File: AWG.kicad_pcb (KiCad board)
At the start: 2 copper layers, 1 part

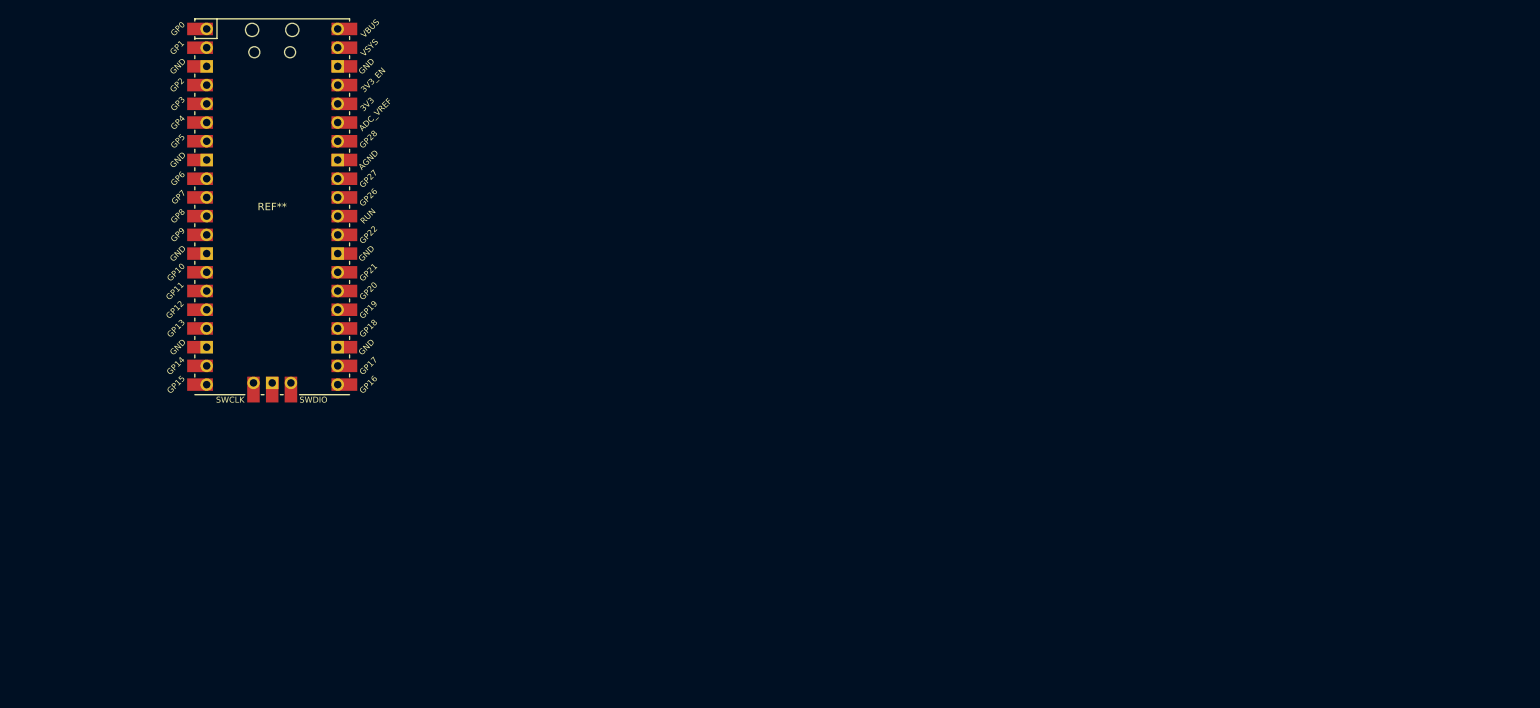
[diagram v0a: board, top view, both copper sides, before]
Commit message: 3D shapes added
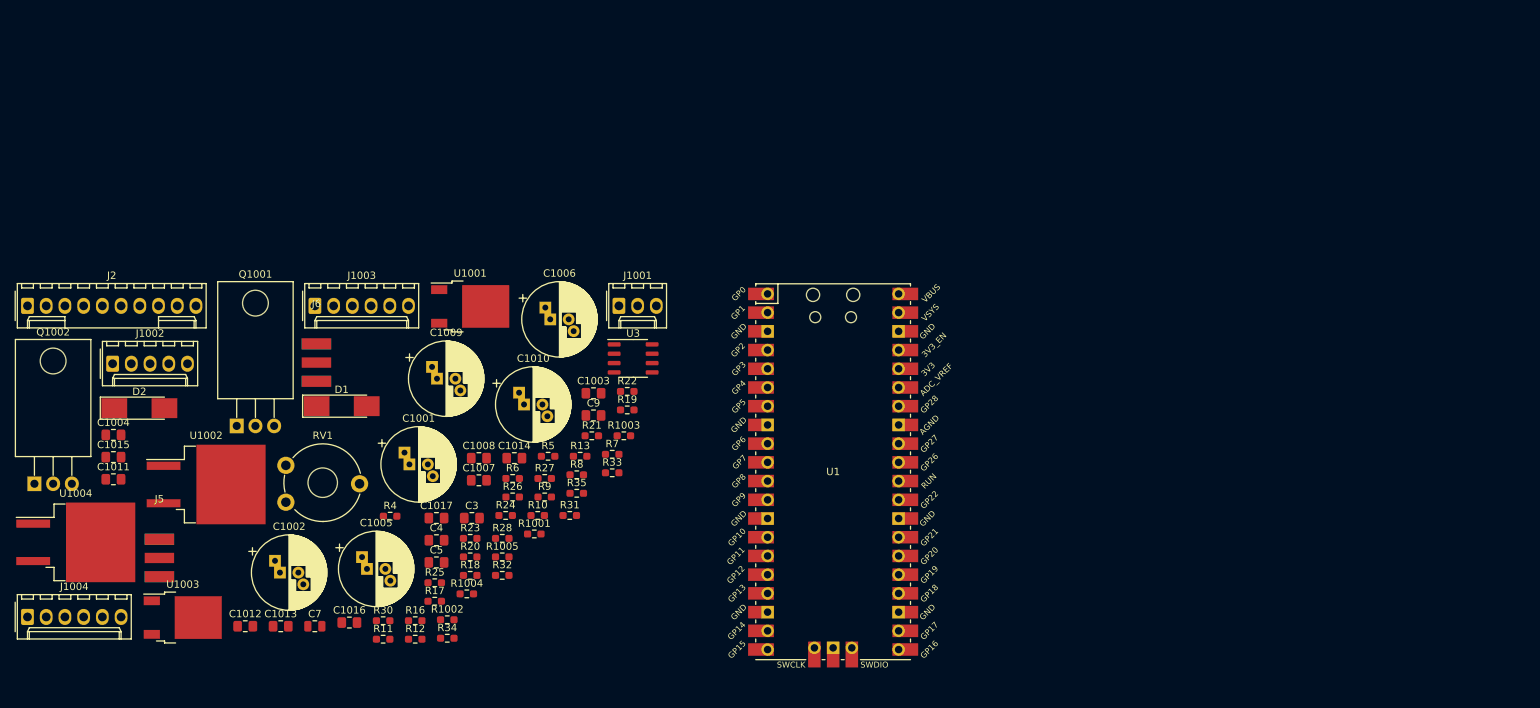
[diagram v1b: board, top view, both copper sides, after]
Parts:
- removed REF**: RPi_Pico_SMD_TH, Pi_Pico:RPi_Pico_SMD_TH
- added C1001: 100u 50V, Capacitor_THT:CP_Radial_D10.0mm_P2.50mm_P5.00mm, F.Cu at (128.6, 95.0)
- added C1002: 100u 50V, Capacitor_THT:CP_Radial_D10.0mm_P2.50mm_P5.00mm, F.Cu at (111.0, 109.6)
- added C1003: 100n, Capacitor_SMD:C_0805_2012Metric_Pad1.18x1.45mm_HandSolder, F.Cu at (153.6, 85.3)
- added C1004: 100n, Capacitor_SMD:C_0805_2012Metric_Pad1.18x1.45mm_HandSolder, F.Cu at (88.5, 91.0)
- added C1005: 100u 50V, Capacitor_THT:CP_Radial_D10.0mm_P2.50mm_P5.00mm, F.Cu at (122.9, 109.1)
- added C1006: 100u 50V, Capacitor_THT:CP_Radial_D10.0mm_P2.50mm_P5.00mm, F.Cu at (147.7, 75.3)
- added C1007: 100n, Capacitor_SMD:C_0805_2012Metric_Pad1.18x1.45mm_HandSolder, F.Cu at (138.0, 97.1)
- added C1008: 100n, Capacitor_SMD:C_0805_2012Metric_Pad1.18x1.45mm_HandSolder, F.Cu at (138.0, 94.1)
- added C1009: 100u 50V, Capacitor_THT:CP_Radial_D10.0mm_P2.50mm_P5.00mm, F.Cu at (132.4, 83.3)
- added C1010: 100u 50V, Capacitor_THT:CP_Radial_D10.0mm_P2.50mm_P5.00mm, F.Cu at (144.2, 86.8)
- added C1011: 100n, Capacitor_SMD:C_0805_2012Metric_Pad1.18x1.45mm_HandSolder, F.Cu at (88.5, 97.0)
- added C1012: 100n, Capacitor_SMD:C_0805_2012Metric_Pad1.18x1.45mm_HandSolder, F.Cu at (106.3, 116.9)
- added C1013: 100n, Capacitor_SMD:C_0805_2012Metric_Pad1.18x1.45mm_HandSolder, F.Cu at (111.2, 116.9)
- added C1014: 100n, Capacitor_SMD:C_0805_2012Metric_Pad1.18x1.45mm_HandSolder, F.Cu at (142.9, 94.1)
- added C1015: 100n, Capacitor_SMD:C_0805_2012Metric_Pad1.18x1.45mm_HandSolder, F.Cu at (88.5, 94.0)
- added C1016: 100n, Capacitor_SMD:C_0805_2012Metric_Pad1.18x1.45mm_HandSolder, F.Cu at (120.5, 116.4)
- added C1017: 100n, Capacitor_SMD:C_0805_2012Metric_Pad1.18x1.45mm_HandSolder, F.Cu at (132.3, 102.2)
- added C3: 100n, Capacitor_SMD:C_0805_2012Metric_Pad1.18x1.45mm_HandSolder, F.Cu at (137.1, 102.2)
- added C4: 100n, Capacitor_SMD:C_0805_2012Metric_Pad1.18x1.45mm_HandSolder, F.Cu at (132.3, 105.2)
- added C5: 100n, Capacitor_SMD:C_0805_2012Metric_Pad1.18x1.45mm_HandSolder, F.Cu at (132.3, 108.3)
- added C7: 3.3p, Capacitor_SMD:C_0805_2012Metric, F.Cu at (115.8, 116.9)
- added C9: 100n, Capacitor_SMD:C_0805_2012Metric_Pad1.18x1.45mm_HandSolder, F.Cu at (153.6, 88.3)
- added D1: 4148, Diode_SMD:D_MELF_Handsoldering, F.Cu at (119.4, 87.1)
- added D2: 4148, Diode_SMD:D_MELF_Handsoldering, F.Cu at (92.0, 87.3)
- added J1001: Conn_01x03, Connector_Molex:Molex_KK-254_AE-6410-03A_1x03_P2.54mm_Vertical, F.Cu at (157.0, 73.4)
- added J1002: Conn_01x05, Connector_Molex:Molex_KK-254_AE-6410-05A_1x05_P2.54mm_Vertical, F.Cu at (88.3, 81.3)
- added J1003: Conn_01x06, Connector_Molex:Molex_KK-254_AE-6410-06A_1x06_P2.54mm_Vertical, F.Cu at (115.8, 73.4)
- added J1004: Conn_01x06, Connector_Molex:Molex_KK-254_AE-6410-06A_1x06_P2.54mm_Vertical, F.Cu at (76.8, 115.7)
- added J2: Conn afficheur, Connector_Molex:Molex_KK-254_AE-6410-10A_1x10_P2.54mm_Vertical, F.Cu at (76.8, 73.4)
- added J5: SMA, SMA_PINS:SMA_EDGE_NRW, F.Cu at (94.7, 107.7)
- added J6: SMA, SMA_PINS:SMA_EDGE_NRW, F.Cu at (116.0, 81.1)
- added Q1001: NTE2633, Package_TO_SOT_THT:TO-220-3_Horizontal_TabDown, F.Cu at (105.2, 89.7)
- added Q1002: NTE2634, Package_TO_SOT_THT:TO-220-3_Horizontal_TabDown, F.Cu at (77.7, 97.6)
- added R10: 2k, Resistor_SMD:R_0603_1608Metric_Pad0.98x0.95mm_HandSolder, F.Cu at (146.0, 101.9)
- added R1001: 1k, Resistor_SMD:R_0603_1608Metric_Pad0.98x0.95mm_HandSolder, F.Cu at (145.6, 104.4)
- added R1002: 1k, Resistor_SMD:R_0603_1608Metric_Pad0.98x0.95mm_HandSolder, F.Cu at (133.8, 116.0)
- added R1003: 1k, Resistor_SMD:R_0603_1608Metric_Pad0.98x0.95mm_HandSolder, F.Cu at (157.7, 91.1)
- added R1004: 1k, Resistor_SMD:R_0603_1608Metric_Pad0.98x0.95mm_HandSolder, F.Cu at (136.4, 112.5)
- added R1005: 1k, Resistor_SMD:R_0603_1608Metric_Pad0.98x0.95mm_HandSolder, F.Cu at (141.2, 107.5)
- added R11: 2k, Resistor_SMD:R_0603_1608Metric_Pad0.98x0.95mm_HandSolder, F.Cu at (125.1, 118.7)
- added R12: 2k, Resistor_SMD:R_0603_1608Metric_Pad0.98x0.95mm_HandSolder, F.Cu at (129.4, 118.7)
- added R13: 2k, Resistor_SMD:R_0603_1608Metric_Pad0.98x0.95mm_HandSolder, F.Cu at (151.8, 93.9)
- added R16: 1k, Resistor_SMD:R_0603_1608Metric_Pad0.98x0.95mm_HandSolder, F.Cu at (129.4, 116.2)
- added R17: 1k, Resistor_SMD:R_0603_1608Metric_Pad0.98x0.95mm_HandSolder, F.Cu at (132.1, 113.5)
- added R18: 1k, Resistor_SMD:R_0603_1608Metric_Pad0.98x0.95mm_HandSolder, F.Cu at (136.9, 110.0)
- added R19: 1k, Resistor_SMD:R_0603_1608Metric_Pad0.98x0.95mm_HandSolder, F.Cu at (158.2, 87.6)
- added R20: 1k, Resistor_SMD:R_0603_1608Metric_Pad0.98x0.95mm_HandSolder, F.Cu at (136.9, 107.5)
- added R21: 1k, Resistor_SMD:R_0603_1608Metric_Pad0.98x0.95mm_HandSolder, F.Cu at (153.4, 91.1)
- added R22: 1k, Resistor_SMD:R_0603_1608Metric_Pad0.98x0.95mm_HandSolder, F.Cu at (158.2, 85.1)
- added R23: 1k, Resistor_SMD:R_0603_1608Metric_Pad0.98x0.95mm_HandSolder, F.Cu at (136.9, 105.0)
- added R24: 1k, Resistor_SMD:R_0603_1608Metric_Pad0.98x0.95mm_HandSolder, F.Cu at (141.7, 101.9)
- added R25: 2k, Resistor_SMD:R_0603_1608Metric_Pad0.98x0.95mm_HandSolder, F.Cu at (132.1, 111.0)
- added R26: 20k, Resistor_SMD:R_0603_1608Metric_Pad0.98x0.95mm_HandSolder, F.Cu at (142.6, 99.4)
- added R27: 680R, Resistor_SMD:R_0603_1608Metric_Pad0.98x0.95mm_HandSolder, F.Cu at (147.0, 96.9)
- added R28: 680R, Resistor_SMD:R_0603_1608Metric_Pad0.98x0.95mm_HandSolder, F.Cu at (141.2, 105.0)
- added R30: 27R, Resistor_SMD:R_0603_1608Metric_Pad0.98x0.95mm_HandSolder, F.Cu at (125.1, 116.2)
- added R31: 1k, Resistor_SMD:R_0603_1608Metric_Pad0.98x0.95mm_HandSolder, F.Cu at (150.4, 101.9)
- added R32: 1k, Resistor_SMD:R_0603_1608Metric_Pad0.98x0.95mm_HandSolder, F.Cu at (141.2, 110.0)
- added R33: 3R3, Resistor_SMD:R_0603_1608Metric_Pad0.98x0.95mm_HandSolder, F.Cu at (156.1, 96.1)
- added R34: 3R3, Resistor_SMD:R_0603_1608Metric_Pad0.98x0.95mm_HandSolder, F.Cu at (133.8, 118.5)
- added R35: 47R, Resistor_SMD:R_0603_1608Metric_Pad0.98x0.95mm_HandSolder, F.Cu at (151.3, 98.9)
- added R4: 2k, Resistor_SMD:R_0603_1608Metric_Pad0.98x0.95mm_HandSolder, F.Cu at (126.0, 102.0)
- added R5: 2k, Resistor_SMD:R_0603_1608Metric_Pad0.98x0.95mm_HandSolder, F.Cu at (147.4, 93.9)
- added R6: 2k, Resistor_SMD:R_0603_1608Metric_Pad0.98x0.95mm_HandSolder, F.Cu at (142.6, 96.9)
- added R7: 2k, Resistor_SMD:R_0603_1608Metric_Pad0.98x0.95mm_HandSolder, F.Cu at (156.1, 93.6)
- added R8: 2k, Resistor_SMD:R_0603_1608Metric_Pad0.98x0.95mm_HandSolder, F.Cu at (151.3, 96.4)
- added R9: 2k, Resistor_SMD:R_0603_1608Metric_Pad0.98x0.95mm_HandSolder, F.Cu at (147.0, 99.4)
- added RV1: 100R, Potentiometer_THT:Potentiometer_Piher_PT-10-V10_Vertical_Hole, F.Cu at (111.9, 100.1)
- added U1: Pico, Pi_Pico:RPi_Pico_SMD_TH, F.Cu at (186.1, 96.0)
- added U1001: L7812, Package_TO_SOT_SMD:TO-252-2, F.Cu at (136.9, 73.5)
- added U1002: L7912, Package_TO_SOT_SMD:TO-263-2, F.Cu at (101.0, 97.7)
- added U1003: L7805, Package_TO_SOT_SMD:TO-252-2, F.Cu at (97.9, 115.7)
- added U1004: L7905, Package_TO_SOT_SMD:TO-263-2, F.Cu at (83.3, 105.5)
- added U3: AD8055ARZ, Package_SO:SO-8_3.9x4.9mm_P1.27mm, F.Cu at (159.0, 80.6)

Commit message: heatsink added
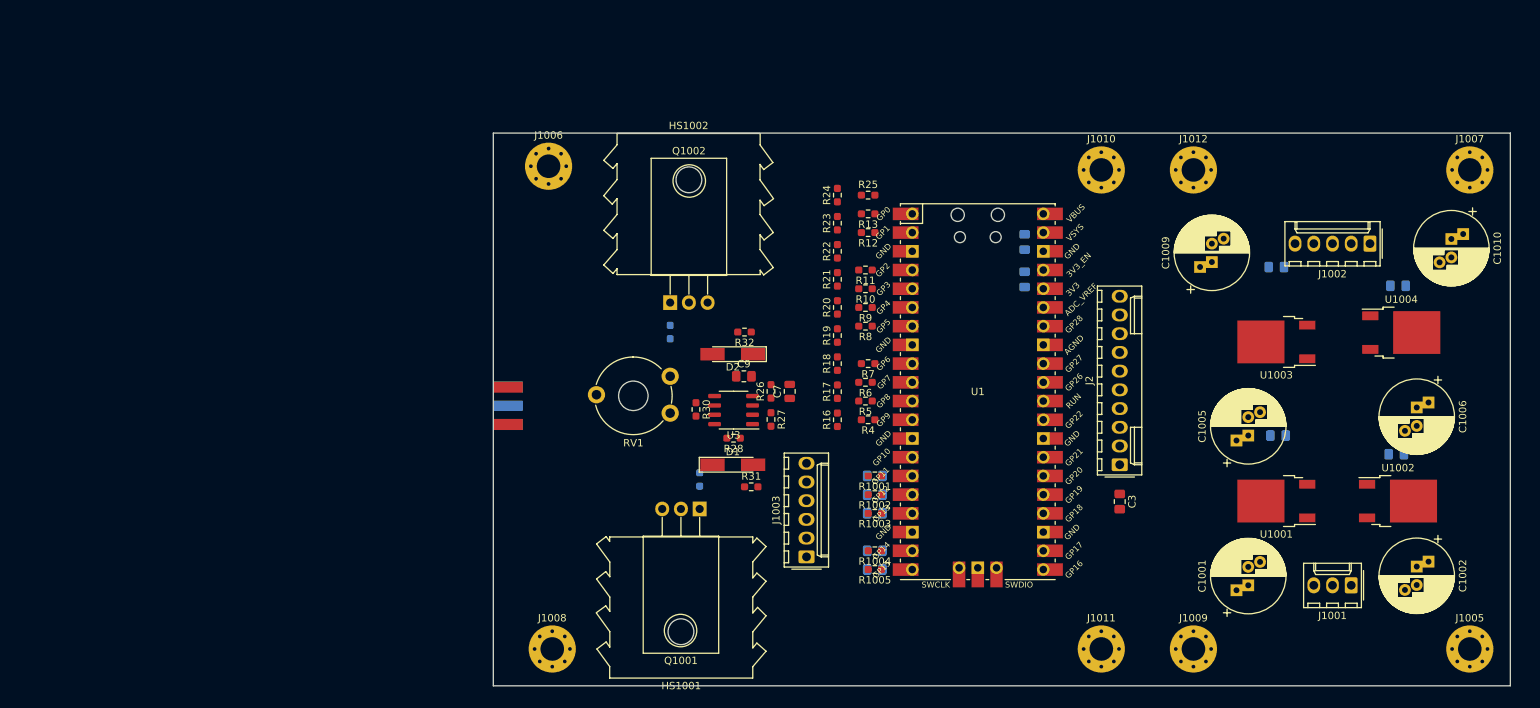
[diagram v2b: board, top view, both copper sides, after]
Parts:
- removed C1014, C1016: 100n, Capacitor_SMD:C_0805_2012Metric_Pad1.18x1.45mm_HandSolder
- removed J1004: Conn_01x06, Connector_Molex:Molex_KK-254_AE-6410-06A_1x06_P2.54mm_Vertical
- removed J6: SMA, SMA_PINS:SMA_EDGE_NRW
- removed R35: 47R, Resistor_SMD:R_0603_1608Metric_Pad0.98x0.95mm_HandSolder
- added HS1001: Heatsink, Heatsink:Heatsink_Aavid-TV5G_TO220_Horizontal, F.Cu at (165.5, 117.5)
- added HS1002: Heatsink, Heatsink:Heatsink_Aavid-TV5G_TO220_Horizontal, F.Cu at (166.5, 56.5)
- added J1005: Conn_01x01, MountingHole:MountingHole_3.2mm_M3_Pad_Via, F.Cu at (272.5, 120.0)
- added J1006: Conn_01x01, MountingHole:MountingHole_3.2mm_M3_Pad_Via, F.Cu at (147.5, 54.5)
- added J1007: Conn_01x01, MountingHole:MountingHole_3.2mm_M3_Pad_Via, F.Cu at (272.5, 55.0)
- added J1008: Conn_01x01, MountingHole:MountingHole_3.2mm_M3_Pad_Via, F.Cu at (148.0, 120.0)
- added J1009: Conn_01x01, MountingHole:MountingHole_3.2mm_M3_Pad_Via, F.Cu at (235.0, 120.0)
- added J1010: Conn_01x01, MountingHole:MountingHole_3.2mm_M3_Pad_Via, F.Cu at (222.5, 55.0)
- added J1011: Conn_01x01, MountingHole:MountingHole_3.2mm_M3_Pad_Via, F.Cu at (222.5, 120.0)
- added J1012: Conn_01x01, MountingHole:MountingHole_3.2mm_M3_Pad_Via, F.Cu at (235.0, 55.0)
- C1003, C1004, C1007, C1008, C1011, C1012, C1013, C1015, C1017, C4, C5, J5, R33, R34: moved to B.Cu
- D1, D2: footprint Diode_SMD:D_MELF_Handsoldering -> Diode_SMD:D_MiniMELF_Handsoldering
- U1002, U1004: footprint Package_TO_SOT_SMD:TO-263-2 -> Package_TO_SOT_SMD:TO-252-2
- moved U1004 182.1 mm to (263.2, 77.1)
- moved C1004 174.1 mm to (262.5, 93.6)
- moved J1002 171.4 mm to (258.9, 65.0), turned to 180 degrees
- moved U1002 161.7 mm to (262.8, 99.9)
- moved C1002 154.3 mm to (265.3, 108.8), turned to 270 degrees
- moved U1003 153.0 mm to (246.2, 78.3), turned to 180 degrees
- moved J2 149.8 mm to (225.0, 95.0), turned to 90 degrees
- moved C1010 127.8 mm to (270.0, 64.4), turned to 270 degrees
- moved C1008 126.9 mm to (262.8, 70.7)
- moved C1005 120.9 mm to (242.4, 91.0), turned to 90 degrees
- moved C1006 118.2 mm to (265.3, 87.2), turned to 270 degrees
- moved C1001 115.0 mm to (242.4, 111.4), turned to 90 degrees
- moved U1001 112.5 mm to (246.2, 99.9), turned to 180 degrees
- moved C1007 112.0 mm to (246.2, 68.2)
- moved J1001 106.4 mm to (256.4, 111.4), turned to 180 degrees
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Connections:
- C1002 pad 1: Net-(C1002-Pad1) -> GND
- C1002 pad 2: GND -> Net-(C1002-Pad2)
- C1006 pad 1: -12V -> GND
- C1006 pad 2: GND -> -12V
- C1010 pad 1: -5V -> GND
- C1010 pad 2: GND -> -5V
- J1001 pad 1: Net-(C1002-Pad1) -> Net-(C1002-Pad2)
- RV1 pad 1: Net-(D1-Pad1) -> Net-(D2-Pad2)
- RV1 pad 3: Net-(D2-Pad2) -> Net-(D1-Pad1)
- U1002 pad 2: Net-(C1002-Pad1) -> Net-(C1002-Pad2)
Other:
- board outline added: 138 x 75 mm

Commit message: routing done
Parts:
- moved C1015 9.27 mm to (201.0, 99.1), turned to 0 degrees
- moved C1017 9.23 mm to (201.0, 96.5), turned to 0 degrees
- moved R28 8.40 mm to (172.6, 83.0)
- moved C1013 8.35 mm to (200.0, 103.0), turned to 270 degrees
- moved C1012 8.34 mm to (200.0, 108.0), turned to 270 degrees
- moved C1011 5.67 mm to (196.0, 113.0)
- moved J1008 3.00 mm to (145.0, 120.0)
- moved R24 2.85 mm to (189.0, 60.1), turned to 270 degrees
- moved J1005 2.50 mm to (275.0, 120.0)
- moved J1006 2.50 mm to (145.0, 54.5)
- moved J1007 2.50 mm to (275.0, 55.0)
- moved R13 2.35 mm to (193.0, 60.0), turned to 270 degrees
- moved C9 2.00 mm to (176.0, 83.0), turned to 270 degrees
- moved R25 1.59 mm to (191.0, 60.0), turned to 90 degrees
- moved R26 0.57 mm to (178.2, 85.0)
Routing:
- net -12V: track 0.00 -> 198.9 mm
- net +5V: track 0.00 -> 181.3 mm
- net +12V: track 0.00 -> 169.1 mm
- net -5V: track 0.00 -> 152.7 mm
- net +3V3: track 0.00 -> 95.4 mm
- net Net-(J5-Pad1): track 0.00 -> 52.5 mm
- net GND: track 0.00 -> 38.0 mm, vias 0 -> 23
- net Net-(J2-Pad2): track 0.00 -> 30.3 mm
- net Net-(C1002-Pad2): track 0.00 -> 24.4 mm
- net Net-(C1011-Pad1): track 0.00 -> 23.1 mm
- net Net-(J2-Pad6): track 0.00 -> 22.7 mm
- net Net-(J2-Pad8): track 0.00 -> 22.6 mm
- net Net-(J2-Pad5): track 0.00 -> 22.6 mm
- net Net-(C1012-Pad1): track 0.00 -> 22.5 mm
- net Net-(J2-Pad7): track 0.00 -> 22.4 mm
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- added copper zone on B.Cu, net GND
- added copper zone on F.Cu, net GND
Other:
- board size 138 x 75 mm -> 140 x 75 mm
- board text added: "+12V +5V GND -5V -12V"
- board text added: "+15V -15V Power In"
- board text added: "Display"
- board text added: "Output"
- board text added: "To Frontpanel"

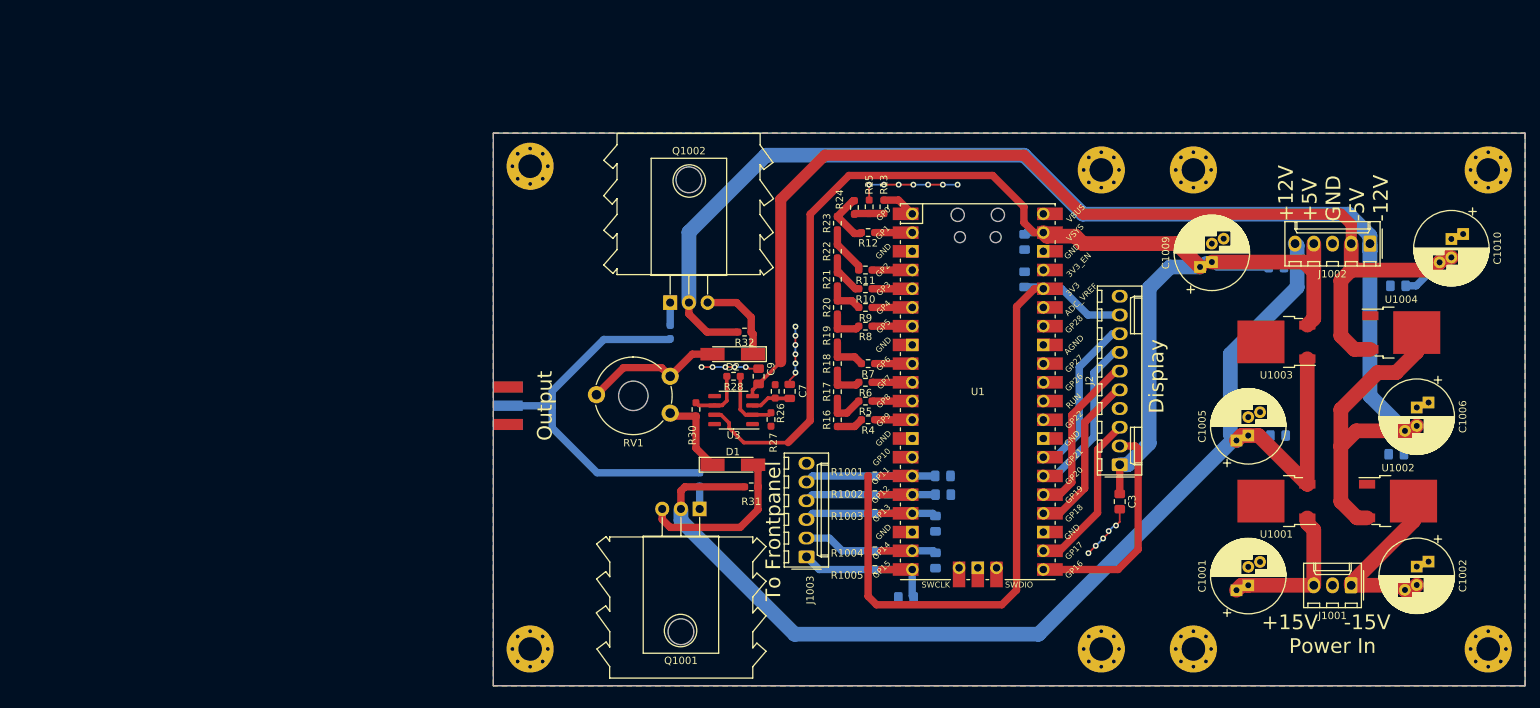
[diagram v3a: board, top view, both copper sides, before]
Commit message: auxiliary power connector added
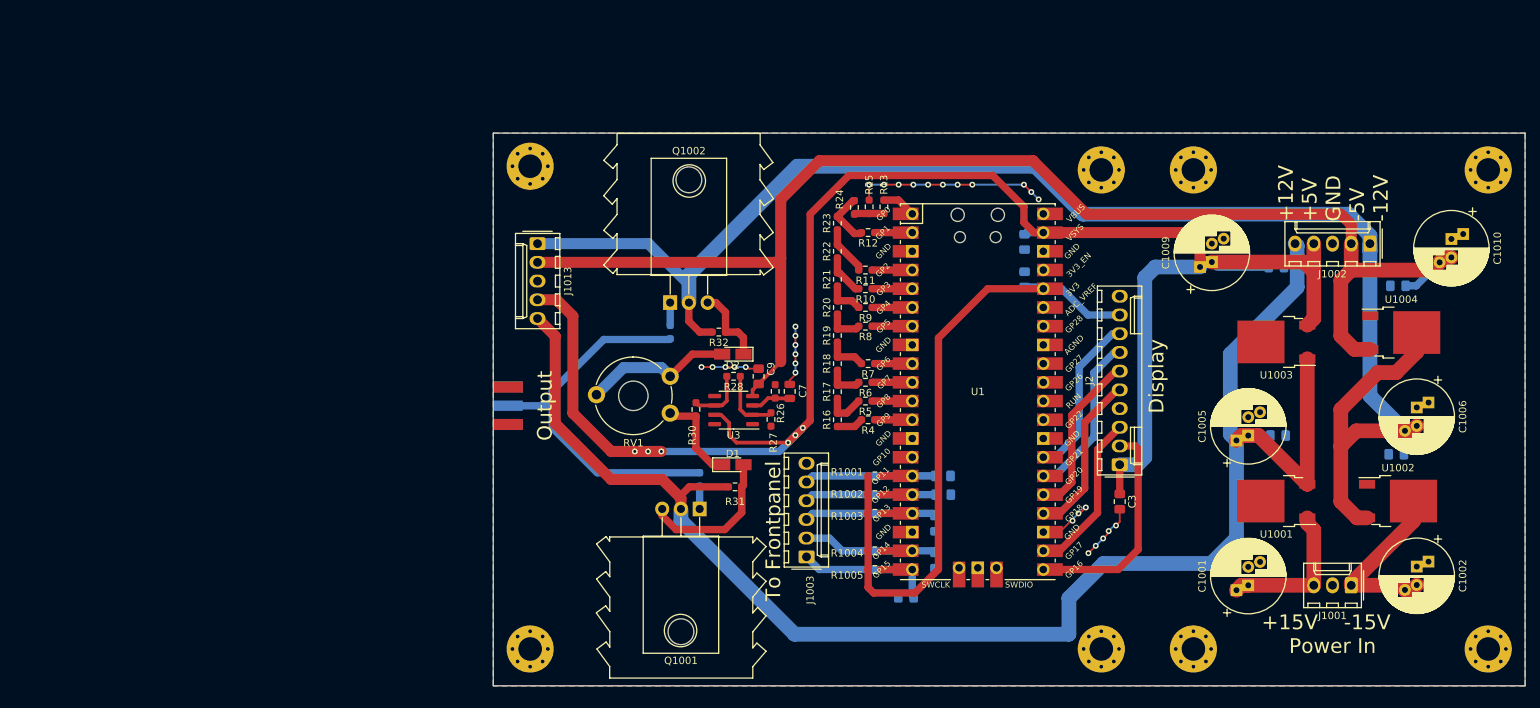
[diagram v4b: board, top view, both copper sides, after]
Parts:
- added J1013: Conn_01x05, Connector_Molex:Molex_KK-254_AE-6410-05A_1x05_P2.54mm_Vertical, F.Cu at (146.0, 65.0)
- D1, D2: footprint Diode_SMD:D_MiniMELF_Handsoldering -> Diode_SMD:D_MicroMELF_Handsoldering
- moved R32 3.49 mm to (170.6, 77.0)
- moved R31 2.20 mm to (172.8, 98.0)
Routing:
- net +5V: track 181.3 -> 242.2 mm, vias 0 -> 6
- net +12V: track 169.1 -> 213.6 mm
- net -5V: track 152.7 -> 185.3 mm
- net GND: track 38.0 -> 57.1 mm, vias 23 -> 30
- net -12V: track 198.9 -> 216.7 mm
- net +3V3: track 95.4 -> 89.2 mm
- net Net-(D1-Pad2): track 22.2 -> 20.0 mm
- net Net-(D2-Pad2): track 19.0 -> 20.3 mm
- net Net-(D1-Pad1): track 11.2 -> 12.5 mm
- net Net-(D2-Pad1): track 11.9 -> 10.7 mm
